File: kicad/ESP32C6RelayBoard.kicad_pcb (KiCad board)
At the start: 2 copper layers, 110.5 x 85.5 mm, 124 parts, among them IC1 SPX1117M3-L-3-3_TR, J1 Screw_Terminal_01x02, J10 Screw_Terminal_01x03, J11 Screw_Terminal_01x03, J12 Screw_Terminal_01x03, J13 Screw_Terminal_01x03, J2 Conn_02x09_Odd_Even, J3 Screw_Terminal_01x02, J4 Screw_Terminal_01x02, J5 10118192-0001LF, J6 Screw_Terminal_01x02, J7 Screw_Terminal_01x02, J8 Screw_Terminal_01x03, J9 Screw_Terminal_01x03, K1 G5RL-K1-E-DC12, K2 G5RL-K1-E-DC12, K3 G5RL-K1-E-DC12, K4 G5RL-K1-E-DC12, Q1 FDN302P, U1 AP62300Z6-7, U10 INA232AIDDFR, U11 74HC237, U12 INA232AIDDFR, U13 FAN3241TMX, U14 FAN3241TMX, U2 ESP32-C6-MINI-1/U, U3 434133025816, U4 434133025816, U5 ESD401DPYR, U6 ESD401DPYR, U7 ESD401DPYR, U8 FAN3241TMX, U9 FAN3241TMX

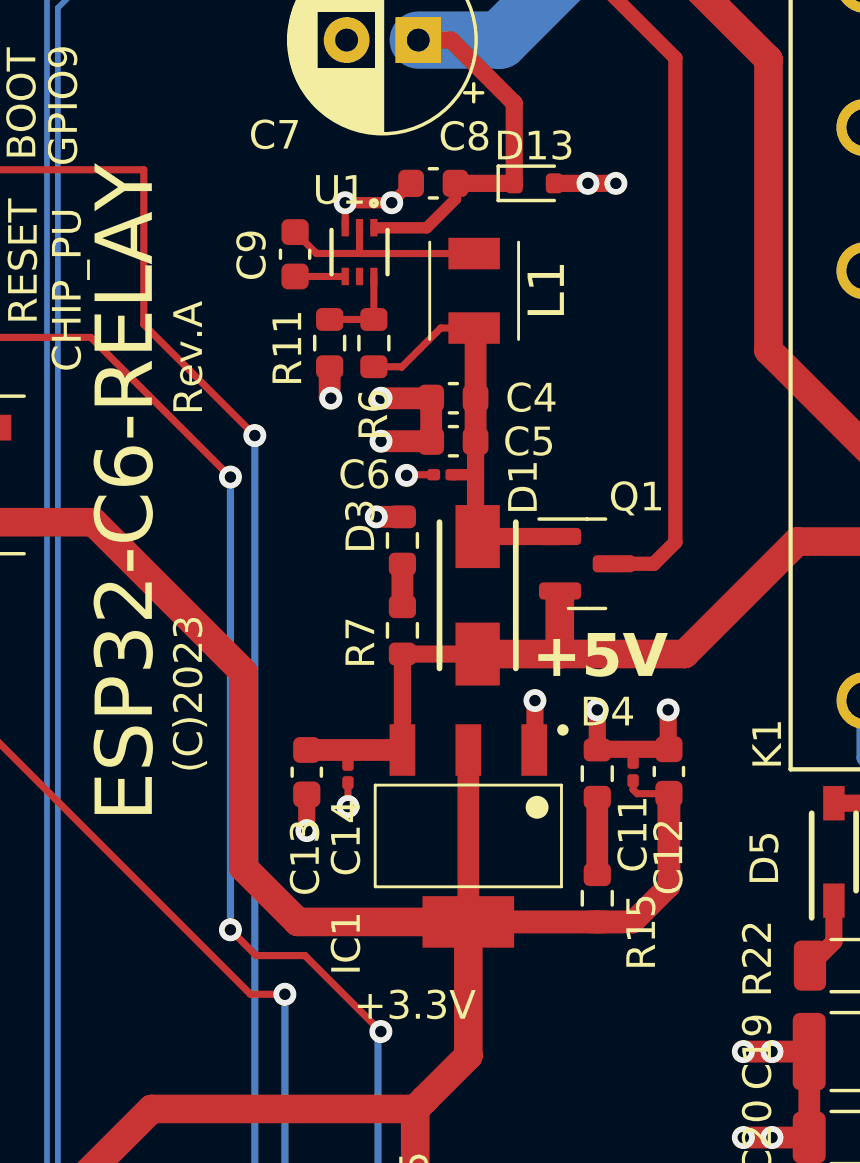
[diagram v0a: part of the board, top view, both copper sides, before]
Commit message: Added oversised thermal pads
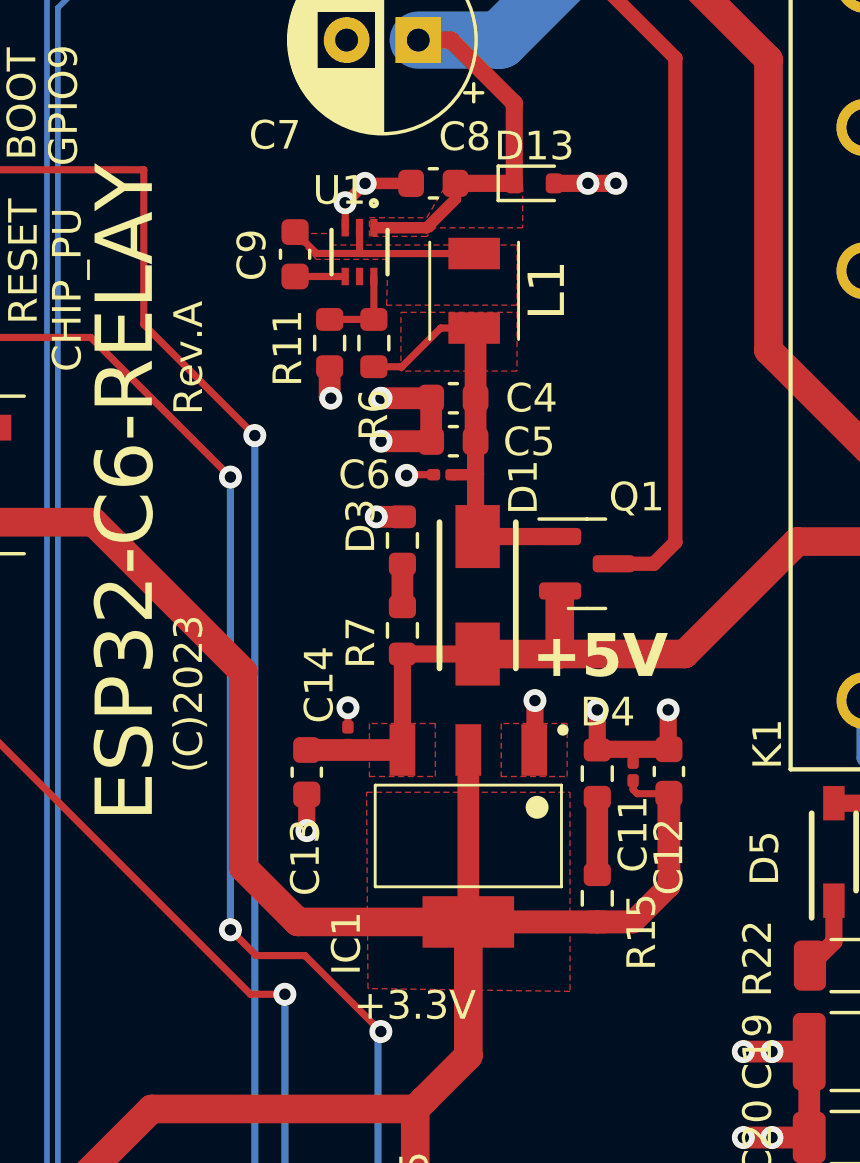
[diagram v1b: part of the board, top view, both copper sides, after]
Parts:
- moved C14 1.30 mm to (68.5, 56.6), turned to 90 degrees
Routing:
- added copper zone on F.Cu, net +12V
- added copper zone on F.Cu, net +3V3
- added copper zone on F.Cu, net +5V
- added copper zone on F.Cu, net GND
- added copper zone on F.Cu, net Net-(D1-A)
- added copper zone on F.Cu, net Net-(U1-SW)

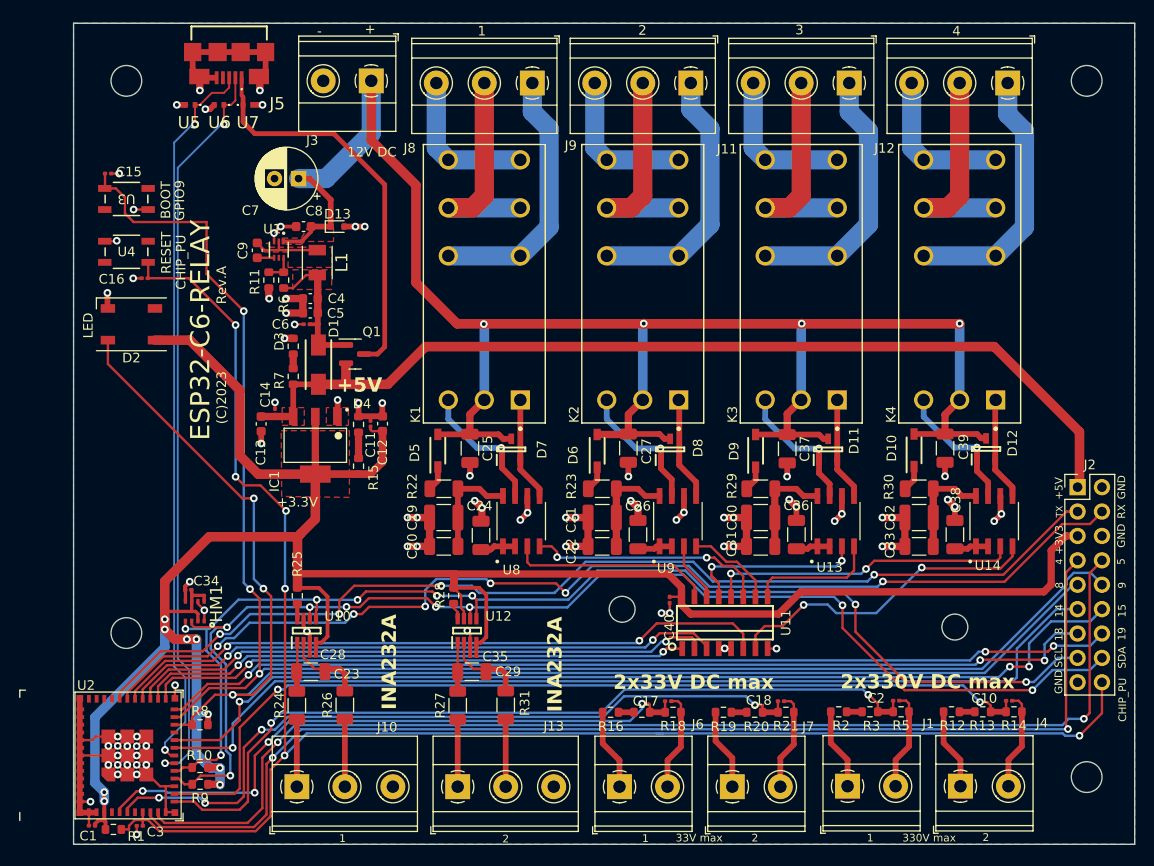
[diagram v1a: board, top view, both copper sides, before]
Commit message: Added power planes.
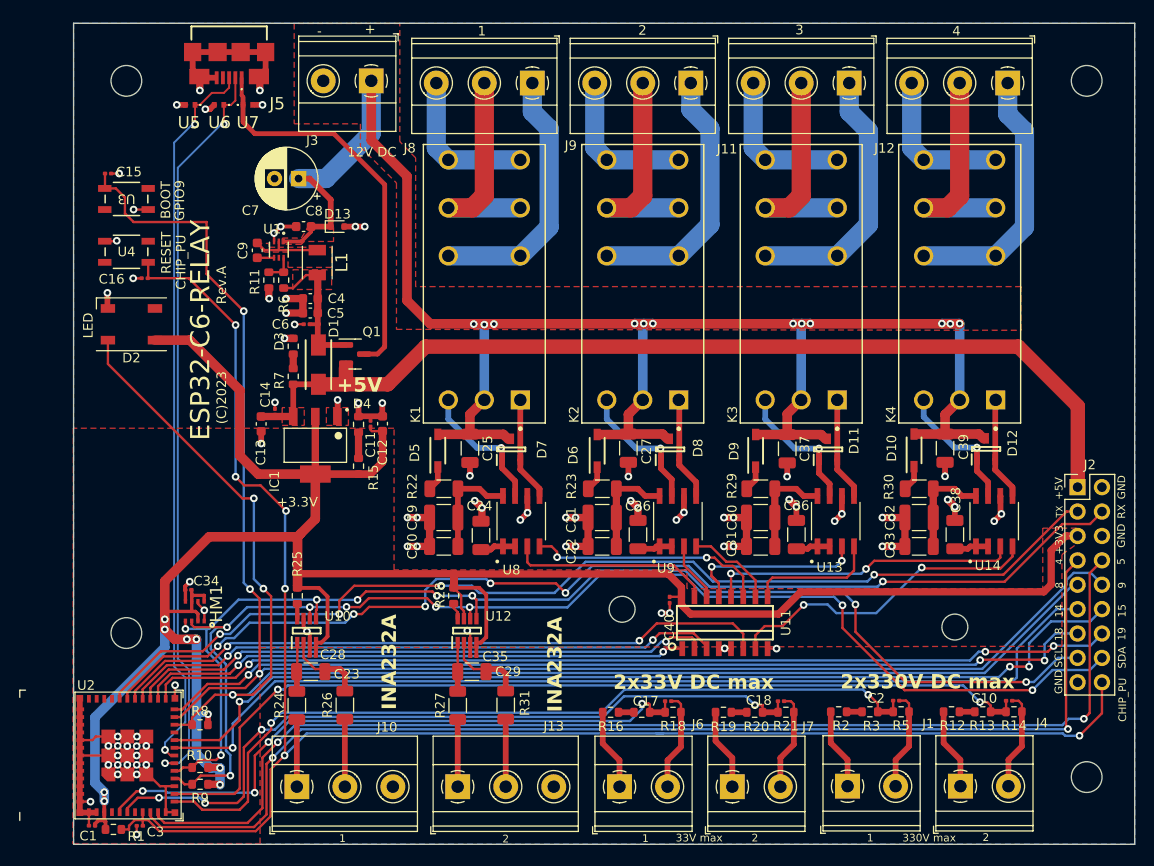
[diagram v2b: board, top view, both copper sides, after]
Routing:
- net +12V: track 188.7 -> 196.0 mm, vias 4 -> 12
- net +5V: track 101.7 -> 102.2 mm
